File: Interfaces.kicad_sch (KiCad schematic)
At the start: 16 parts, among them J1 200528-0100, J2 Conn_01x04_MountingPin, J3 USB4110GFA, J4 BG301-06-X-XXXX-X-X_REVC, J5 BG301-06-X-XXXX-X-X_REVC, U1 USBLC6-2P6, U10 USBLC6-2P6

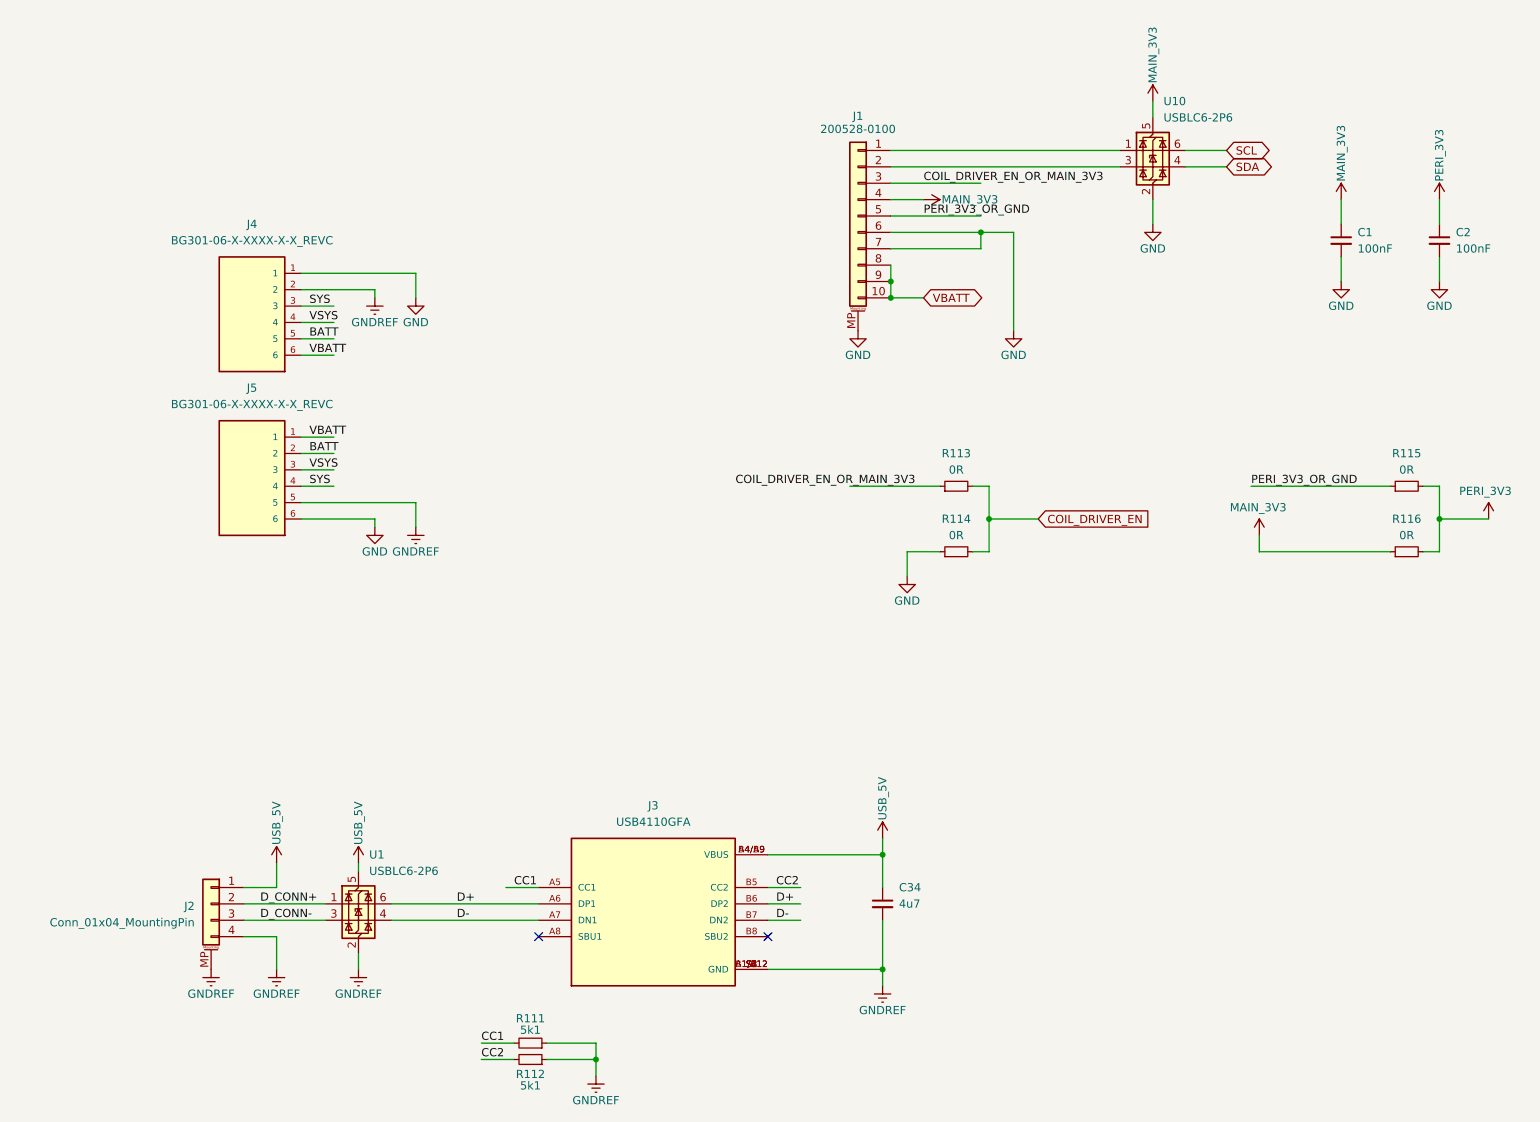
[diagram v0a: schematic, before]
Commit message: Cleaned up silkscreen
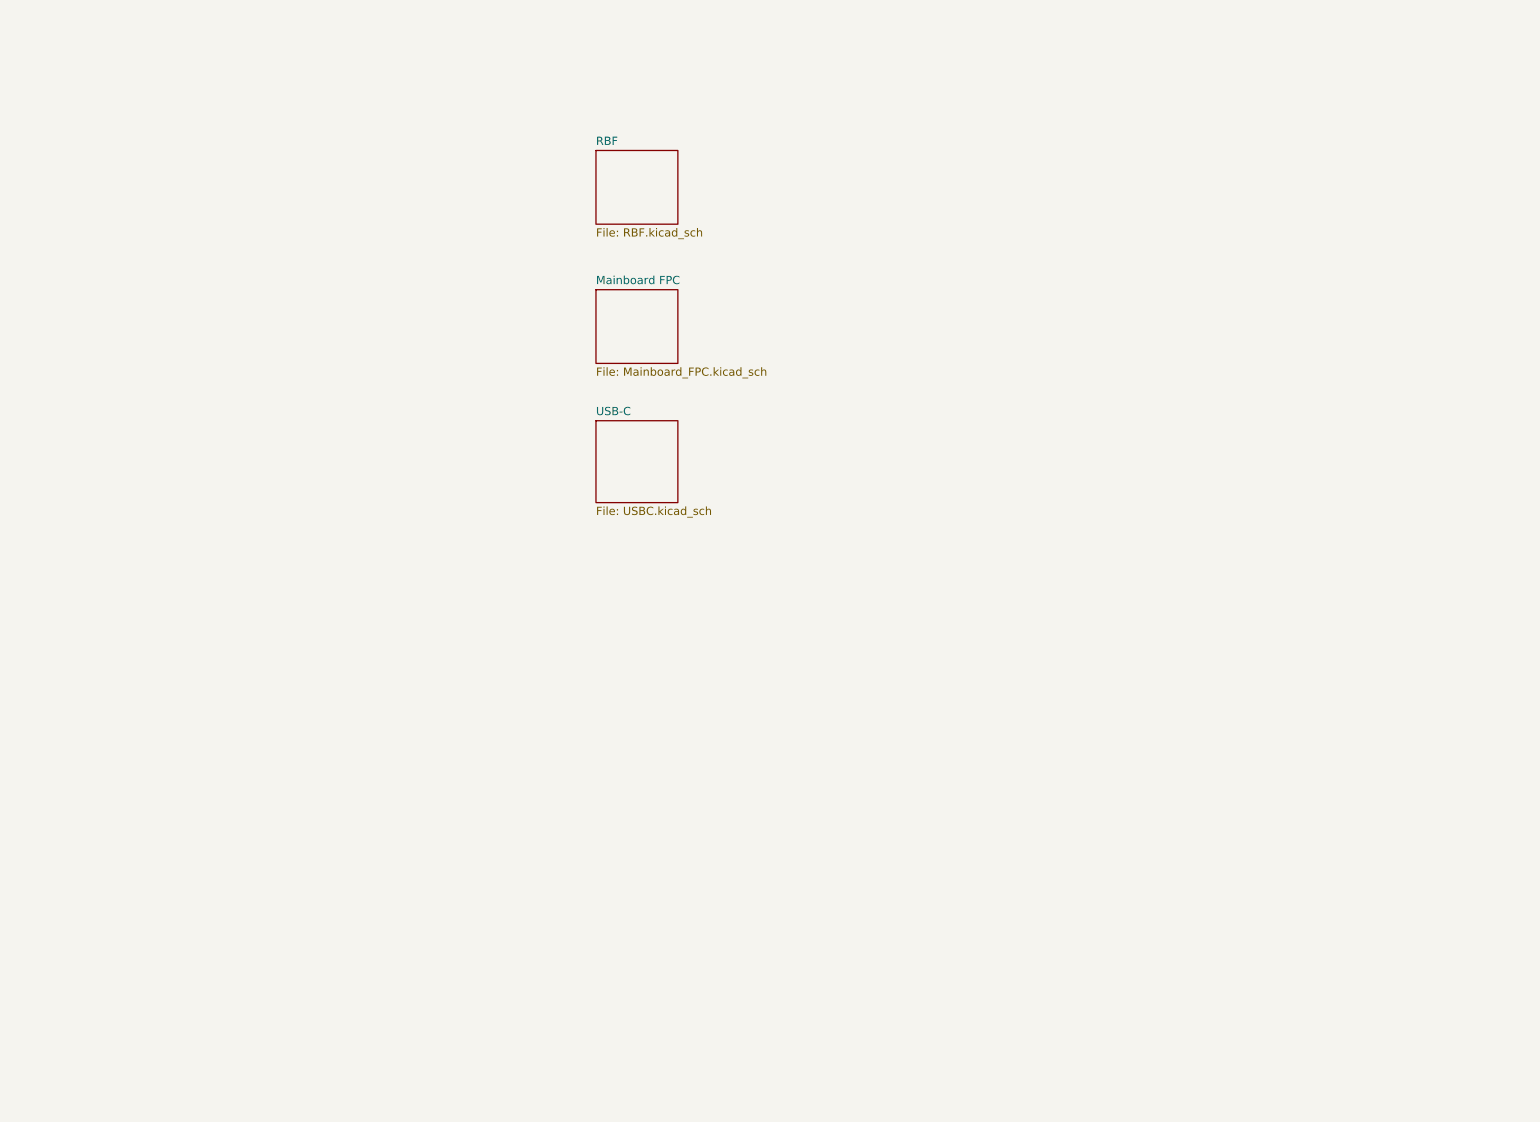
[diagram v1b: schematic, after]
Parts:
- removed C1, C2: 100nF, Capacitor_SMD:C_0603_1608Metric, symbol Device:C_Small
- removed C34: 4u7, Capacitor_SMD:C_0603_1608Metric, symbol Device:C_Small
- removed J1: 200528-0100, Argus-Connectors:Molex_200528-0100_1x10-1MP_P1.00mm_Horizontal, symbol Connector_Generic_MountingPin:Conn_01x10_MountingPin
- removed J2: Conn_01x04_MountingPin, Argus-Connectors:Molex_200528-0040_1x04-1MP_P1.00mm_Horizontal, symbol Connector_Generic_MountingPin:Conn_01x04_MountingPin
- removed J3: USB4110GFA, Argus-Connectors:GCT_USB4110GFA, symbol Argus-Connectors:USB4110GFA
- removed J4, J5: BG301-06-X-XXXX-X-X_REVC, Argus-Connectors:GCT_BG301-06-X-XXXX-X-X_REVC, symbol Argus-Connectors:BG301-06-X-XXXX-X-X_REVC
- removed R111, R112: 5k1, Resistor_SMD:R_0603_1608Metric, symbol Device:R_Small
- removed R113, R114, R115, R116: 0R, Resistor_SMD:R_0603_1608Metric, symbol Device:R_Small
- removed U1, U10: USBLC6-2P6, Package_TO_SOT_SMD:SOT-666, symbol Power_Protection:USBLC6-2P6
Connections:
- no-connect marks 2 -> 0
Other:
- added sheet Mainboard FPC (Mainboard_FPC.kicad_sch)
- added sheet RBF (RBF.kicad_sch)
- added sheet USB-C (USBC.kicad_sch)
